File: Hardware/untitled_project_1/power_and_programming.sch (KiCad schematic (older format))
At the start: 29 parts

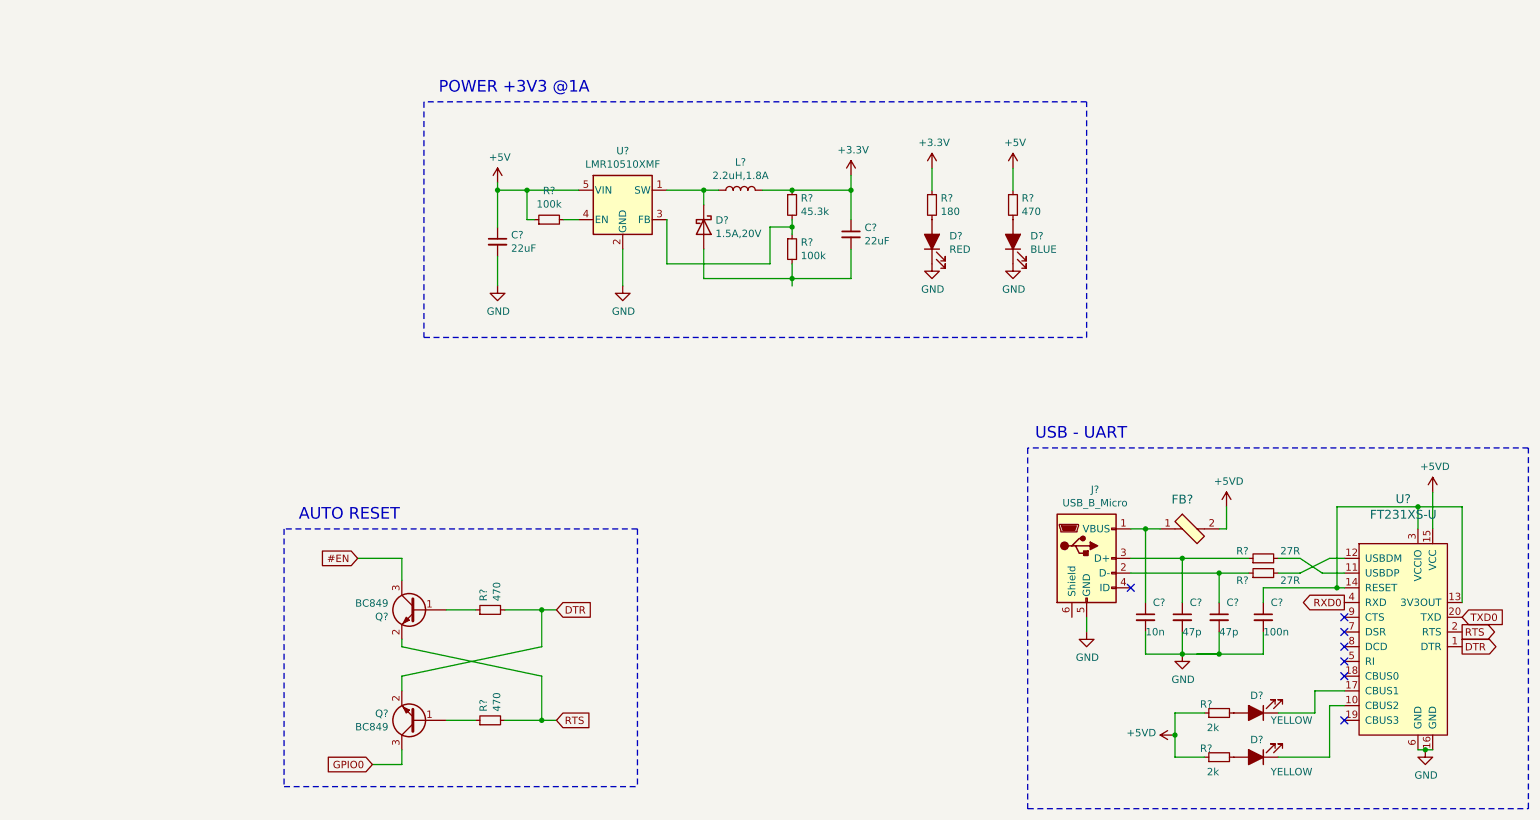
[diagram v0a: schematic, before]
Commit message: add power and programming schematics
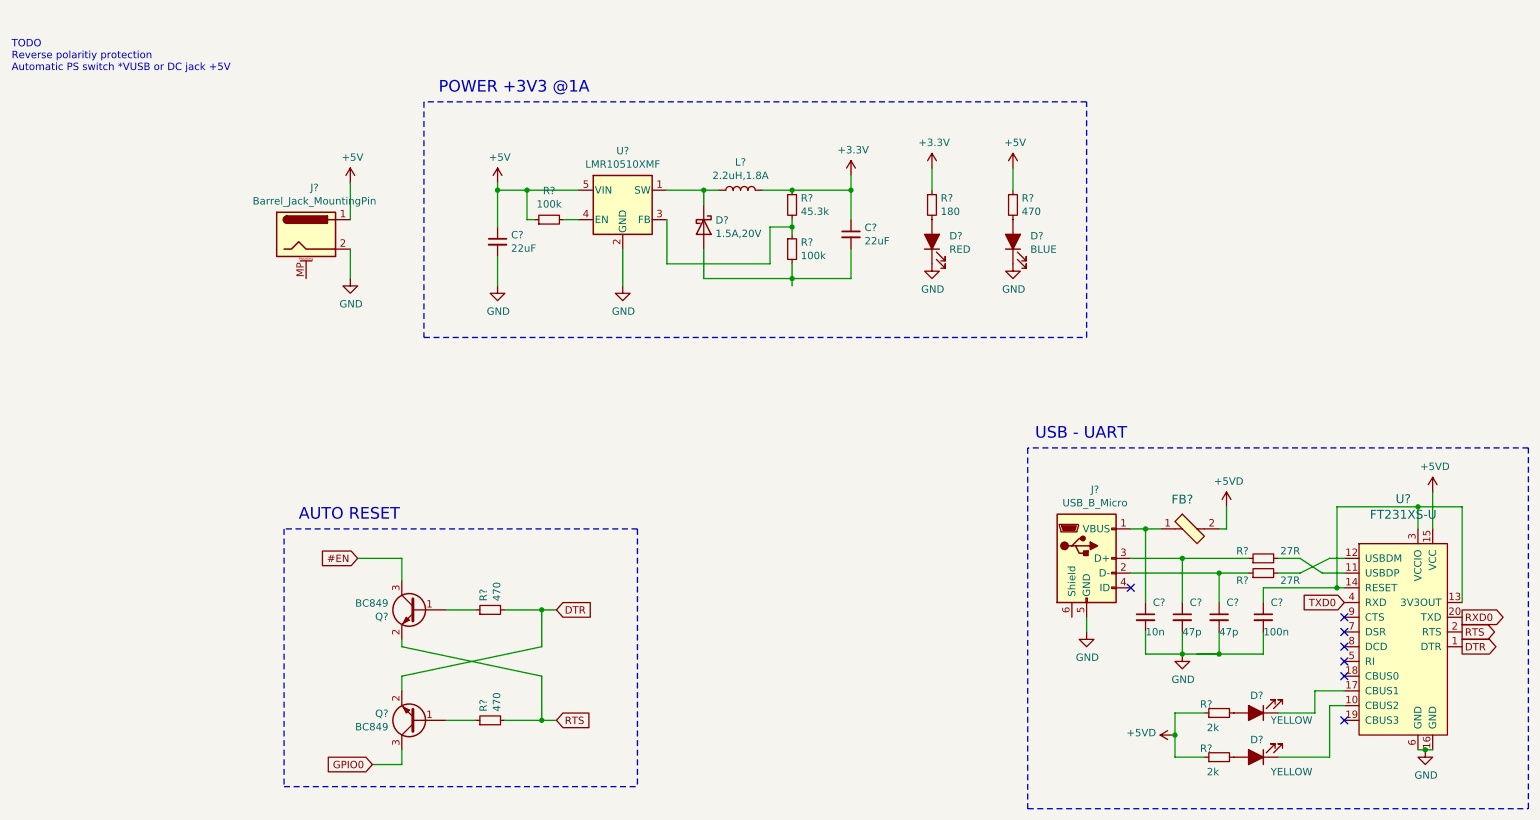
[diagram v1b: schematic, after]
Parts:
- added J?: Barrel_Jack_MountingPin, symbol Connector:Barrel_Jack_MountingPin
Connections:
- net +5V: now also J?.1
- net GND: now also J?.2
- net RXD0: now also U?.20 (TXD); no longer U?.4 (RXD)
- net TXD0: now also U?.4 (RXD); no longer U?.20 (TXD)
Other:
- note added: "TODO\nReverse polaritiy protection\nAutomatic PS switch *VUSB or DC jack +5V\n"
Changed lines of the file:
@@
 $Descr A4 11693 8268
 encoding utf-8
-Sheet 4 4
+Sheet 3 3
 Title ""
 Date ""
@@
 Wire Wire Line
 	8800 5050 9100 5050
-Text GLabel 9650 4700 0    50   Output ~ 0
+Text GLabel 10450 4800 2    50   Output ~ 0
 RXD0
-Text GLabel 10450 4800 2    50   Input ~ 0
+Text GLabel 9650 4700 0    50   Input ~ 0
 TXD0
 Text GLabel 10450 4900 2    50   Output ~ 0
@@
 Wire Notes Line
 	7500 3650 7500 6100
+$Comp
+L Connector:Barrel_Jack_MountingPin J?
+U 1 1 5F07EFAE
+P 2600 2200
+F 0 "J?" H 2657 2517 50  0000 C CNN
+F 1 "Barrel_Jack_MountingPin" H 2657 2426 50  0000 C CNN
+F 2 "" H 2650 2160 50  0001 C CNN
+F 3 "~" H 2650 2160 50  0001 C CNN
+	1    2600 2200
+	1    0    0    -1
+$EndComp
+$Comp
+L power:GND #PWR?
+U 1 1 5F081B0F
+P 2900 2500
+F 0 "#PWR?" H 2900 2250 50  0001 C CNN
+F 1 "GND" H 2905 2327 50  0000 C CNN
+F 2 "" H 2900 2500 50  0001 C CNN
+F 3 "" H 2900 2500 50  0001 C CNN
+	1    2900 2500
+	1    0    0    -1
+$EndComp
+Wire Wire Line
+	2900 2300 2900 2500
+$Comp
+L power:+5V #PWR?
+U 1 1 5F08A07D
+P 2900 1850
+F 0 "#PWR?" H 2900 1700 50  0001 C CNN
+F 1 "+5V" H 2915 2023 50  0000 C CNN
+F 2 "" H 2900 1850 50  0001 C CNN
+F 3 "" H 2900 1850 50  0001 C CNN
+	1    2900 1850
+	1    0    0    -1
+$EndComp
+Wire Wire Line
+	2900 2100 2900 1850
+Text Notes 600  1100 0    50   ~ 0
+TODO\nReverse polaritiy protection\nAutomatic PS switch *VUSB or DC jack +5V\n
 $EndSCHEMATC

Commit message: add footprints to szymbols:
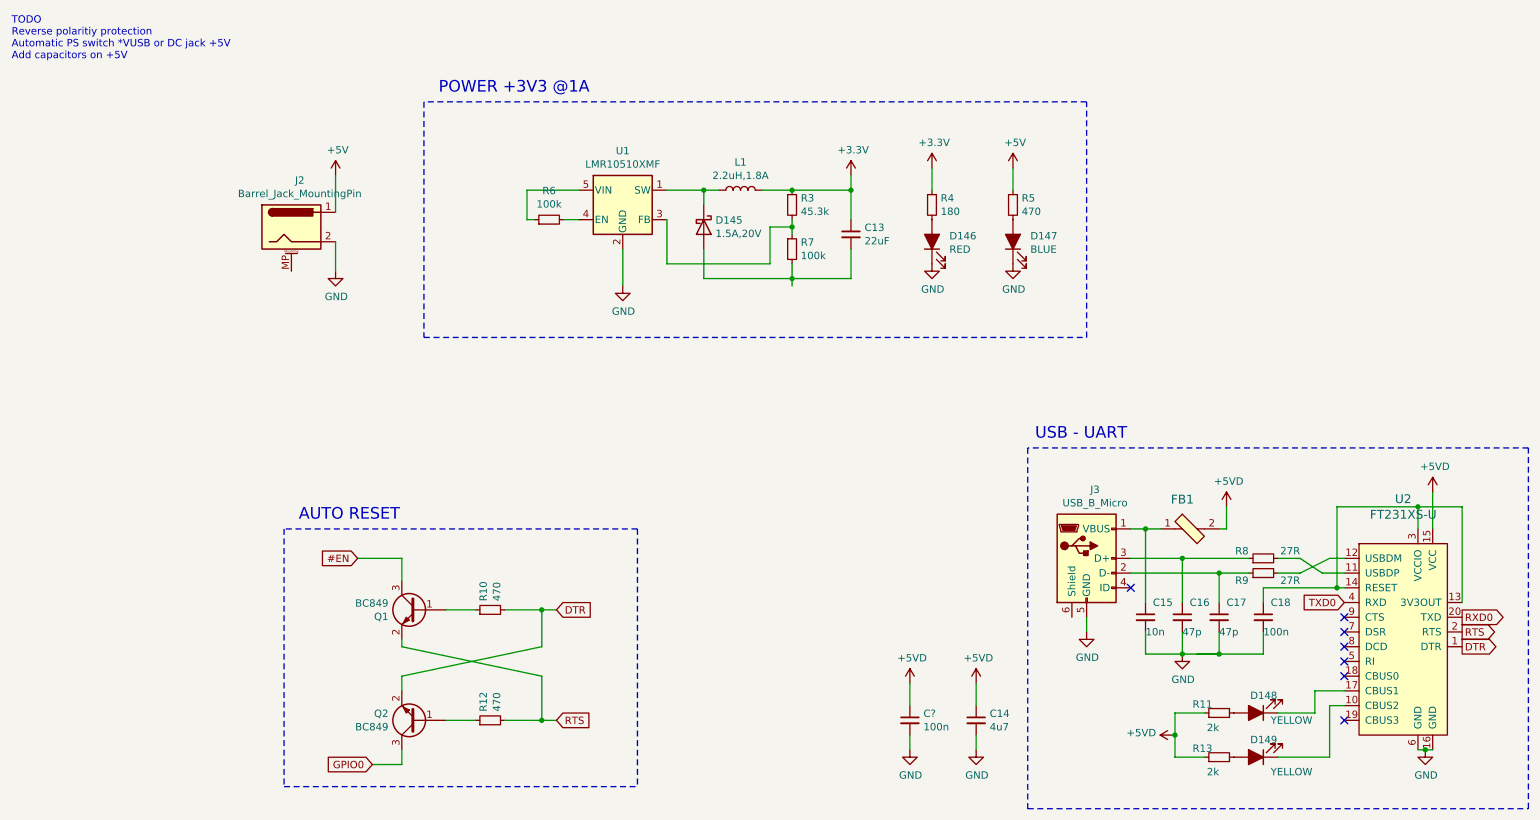
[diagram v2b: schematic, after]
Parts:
- added C?: 100n, Capacitor_SMD:C_1210_3225Metric_Pad1.42x2.65mm_HandSolder, symbol Device:C_Small
- C13, C15, C16, C17, C18: renamed from C?; footprint (none) -> Capacitor_SMD:C_1210_3225Metric_Pad1.42x2.65mm_HandSolder
- C14: renamed from C?; value 22uF -> 4u7; footprint (none) -> Capacitor_SMD:C_1210_3225Metric_Pad1.42x2.65mm_HandSolder
- D145, D146, D147, D148, D149: renamed from D?; footprint (none) -> Diode_SMD:D_1210_3225Metric_Pad1.42x2.65mm_HandSolder
- J3: renamed from J?; footprint (none) -> Connector_USB:USB_Micro-B_Amphenol_10104110_Horizontal
- L1: renamed from L?; footprint (none) -> Inductor_SMD:L_0805_2012Metric_Pad1.15x1.40mm_HandSolder
- R10, R11, R12, R13, R3, R4, R5, R6, R7, R8, R9: renamed from R?; footprint (none) -> Resistor_SMD:R_1210_3225Metric_Pad1.42x2.65mm_HandSolder
- U2: renamed from U?; footprint digikey-footprints:SSOP-20_W3.9mm -> (none)
- gave numbers to parts that had none: 5
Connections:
- net +5V: no longer C14.1, R6.1, U1.5 (VIN)
- net +5VD: now also C14.1, C?.1
- net GND: now also C?.2
- new net: R6.1, U1.5 (VIN)
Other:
- note added: "TODO\nReverse polaritiy protection\nAutomatic PS switch *VUSB or DC jack +5V\nAdd capacitors on +5V\n\n"
- note removed: "TODO\nReverse polaritiy protection\nAutomatic PS switch *VUSB or DC jack +5V\n"
- moved on the sheet: C14, J2
